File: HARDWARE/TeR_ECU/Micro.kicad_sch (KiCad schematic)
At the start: 23 parts, among them J1 Debug, SW1 RST, U1 STM32F446RETx, Y1 Crystal

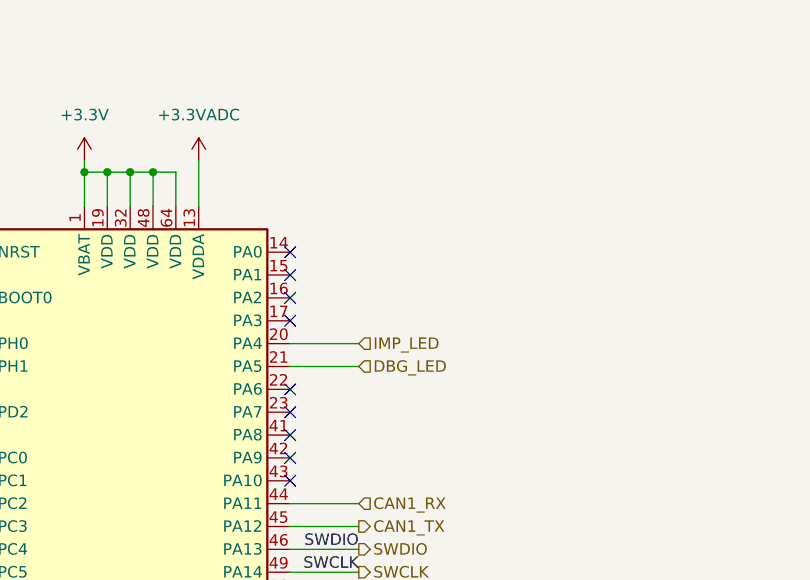
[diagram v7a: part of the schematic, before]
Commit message: Rethought layout and added pulldown to Horn mosfet
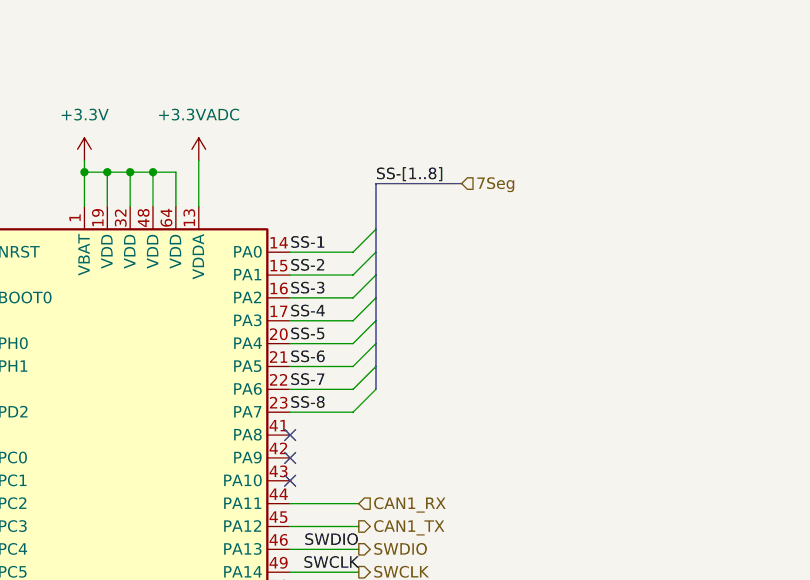
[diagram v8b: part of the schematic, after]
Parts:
- C6: footprint Capacitor_SMD:C_0805_2012Metric -> Capacitor_SMD:C_0402_1005Metric
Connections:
- net SS-1: now reaches U1.14 (PA0)
- net SS-2: now reaches U1.15 (PA1)
- net SS-3: now reaches U1.16 (PA2)
- net SS-4: now reaches U1.17 (PA3)
- net SS-7: now reaches U1.22 (PA6)
- net SS-8: now reaches U1.23 (PA7)
- net DBG_LED renamed SS-6
- net IMP_LED renamed SS-5
- no-connect marks 33 -> 27
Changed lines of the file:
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@@
   (no_connect (at 170.18 81.28))
   (no_connect (at 134.62 114.3))
-  (no_connect (at 170.18 55.88))
   (no_connect (at 134.62 91.44))
-  (no_connect (at 170.18 73.66))
   (no_connect (at 134.62 121.92))
   (no_connect (at 170.18 124.46))
-  (no_connect (at 170.18 63.5))
   (no_connect (at 170.18 127))
-  (no_connect (at 170.18 60.96))
   (no_connect (at 170.18 109.22))
   (no_connect (at 170.18 106.68))
@@
   (no_connect (at 134.62 73.66))
   (no_connect (at 170.18 116.84))
-  (no_connect (at 170.18 58.42))
-  (no_connect (at 170.18 71.12))
   (no_connect (at 170.18 78.74))
   (no_connect (at 134.62 86.36))
   (no_connect (at 134.62 116.84))
+  (bus_entry (at 179.705 68.58) (size -2.54 2.54)
+    (stroke (width 0) (type default))
+  )
+  (bus_entry (at 179.705 53.34) (size -2.54 2.54)
+    (stroke (width 0) (type default))
+  )
+  (bus_entry (at 179.705 60.96) (size -2.54 2.54)
+    (stroke (width 0) (type default))
+  )
+  (bus_entry (at 179.705 63.5) (size -2.54 2.54)
+    (stroke (width 0) (type default))
+  )
+  (bus_entry (at 179.705 55.88) (size -2.54 2.54)
+    (stroke (width 0) (type default))
+  )
+  (bus_entry (at 179.705 71.12) (size -2.54 2.54)
+    (stroke (width 0) (type default))
+  )
+  (bus_entry (at 179.705 66.04) (size -2.54 2.54)
+    (stroke (width 0) (type default))
+  )
+  (bus_entry (at 179.705 58.42) (size -2.54 2.54)
+    (stroke (width 0) (type default))
+  )
   (wire (pts (xy 152.4 46.99) (xy 149.86 46.99))
     (stroke (width 0) (type default))
@@
     (stroke (width 0) (type default))
   )
+  (wire (pts (xy 170.18 66.04) (xy 177.165 66.04))
+    (stroke (width 0) (type default))
+  )
   (wire (pts (xy 34.29 173.99) (xy 38.1 173.99))
     (stroke (width 0) (type default))
@@
     (stroke (width 0) (type default))
   )
-  (wire (pts (xy 170.18 66.04) (xy 177.8 66.04))
+  (bus (pts (xy 179.705 66.04) (xy 179.705 68.58))
+    (stroke (width 0) (type default))
+  )
+  (bus (pts (xy 179.705 58.42) (xy 179.705 60.96))
+    (stroke (width 0) (type default))
+  )
+  (wire (pts (xy 170.18 63.5) (xy 177.165 63.5))
     (stroke (width 0) (type default))
   )
@@
     (stroke (width 0) (type default))
   )
+  (wire (pts (xy 170.18 60.96) (xy 177.165 60.96))
+    (stroke (width 0) (type default))
+  )
   (wire (pts (xy 124.46 66.04) (xy 134.62 66.04))
     (stroke (width 0) (type default))
@@
     (stroke (width 0) (type default))
   )
+  (bus (pts (xy 179.705 53.34) (xy 179.705 55.88))
+    (stroke (width 0) (type default))
+  )
   (polyline (pts (xy 12.7 77.47) (xy 74.93 77.47))
     (stroke (width 0) (type default))
@@
     (stroke (width 0) (type default))
   )
+  (wire (pts (xy 170.18 73.66) (xy 177.165 73.66))
+    (stroke (width 0) (type default))
+  )
   (wire (pts (xy 27.94 91.44) (xy 27.94 88.9))
     (stroke (width 0) (type default))
@@
     (stroke (width 0) (type default))
   )
+  (bus (pts (xy 189.23 48.26) (xy 179.705 48.26))
+    (stroke (width 0) (type default))
+  )
   (wire (pts (xy 38.1 128.27) (xy 38.1 127))
     (stroke (width 0) (type default))
   )
-  (wire (pts (xy 170.18 68.58) (xy 177.8 68.58))
-    (stroke (width 0) (type default))
-  )
   (wire (pts (xy 170.18 91.44) (xy 177.8 91.44))
     (stroke (width 0) (type default))
@@
     (stroke (width 0) (type default))
   )
+  (bus (pts (xy 179.705 63.5) (xy 179.705 66.04))
+    (stroke (width 0) (type default))
+  )
   (wire (pts (xy 33.02 173.99) (xy 34.29 173.99))
     (stroke (width 0) (type default))
@@
     (stroke (width 0) (type default))
   )
+  (wire (pts (xy 170.18 55.88) (xy 177.165 55.88))
+    (stroke (width 0) (type default))
+  )
   (wire (pts (xy 36.83 104.14) (xy 45.72 104.14))
     (stroke (width 0) (type default))
@@
     (stroke (width 0) (type default))
   )
+  (bus (pts (xy 179.705 60.96) (xy 179.705 63.5))
+    (stroke (width 0) (type default))
+  )
   (wire (pts (xy 60.96 128.27) (xy 60.96 127))
     (stroke (width 0) (type default))
@@
     (stroke (width 0) (type default))
   )
+  (bus (pts (xy 179.705 48.26) (xy 179.705 53.34))
+    (stroke (width 0) (type default))
+  )
   (wire (pts (xy 260.35 27.94) (xy 260.35 30.48))
     (stroke (width 0) (type default))
@@
     (stroke (width 0) (type default))
   )
+  (bus (pts (xy 179.705 55.88) (xy 179.705 58.42))
+    (stroke (width 0) (type default))
+  )
   (wire (pts (xy 147.32 45.72) (xy 147.32 46.99))
     (stroke (width 0) (type default))
@@
     (stroke (width 0) (type default))
   )
+  (bus (pts (xy 179.705 68.58) (xy 179.705 71.12))
+    (stroke (width 0) (type default))
+  )
   (wire (pts (xy 52.07 132.08) (xy 52.07 134.62))
     (stroke (width 0) (type default))
   )
+  (wire (pts (xy 170.18 68.58) (xy 177.165 68.58))
+    (stroke (width 0) (type default))
+  )
   (wire (pts (xy 45.72 173.99) (xy 48.26 173.99))
     (stroke (width 0) (type default))
@@
     (stroke (width 0) (type default))
   )
+  (wire (pts (xy 170.18 71.12) (xy 177.165 71.12))
+    (stroke (width 0) (type default))
+  )
   (wire (pts (xy 266.7 38.1) (xy 260.35 38.1))
     (stroke (width 0) (type default))
   )
   (wire (pts (xy 157.48 50.8) (xy 157.48 46.99))
+    (stroke (width 0) (type default))
+  )
+  (wire (pts (xy 170.18 58.42) (xy 177.165 58.42))
     (stroke (width 0) (type default))
   )
@@
     (effects (font (size 1.27 1.27)) (justify right bottom))
   )
+  (label "SS-5" (at 170.18 66.04 0) (fields_autoplaced)
+    (effects (font (size 1.27 1.27)) (justify left bottom))
+  )
   (label "BOOT1" (at 59.69 147.32 180) (fields_autoplaced)
     (effects (font (size 1.27 1.27)) (justify right bottom))
   )
+  (label "SS-[1..8]" (at 179.705 48.26 0) (fields_autoplaced)
+    (effects (font (size 1.27 1.27)) (justify left bottom))
+  )
   (label "OSC_IN" (at 124.46 66.04 0) (fields_autoplaced)
     (effects (font (size 1.27 1.27)) (justify left bottom))
   )
   (label "OSC_OUT" (at 124.46 68.58 0) (fields_autoplaced)
+    (effects (font (size 1.27 1.27)) (justify left bottom))
+  )
+  (label "SS-6" (at 170.18 68.58 0) (fields_autoplaced)
+    (effects (font (size 1.27 1.27)) (justify left bottom))
+  )
+  (label "SS-3" (at 170.18 60.96 0) (fields_autoplaced)
     (effects (font (size 1.27 1.27)) (justify left bottom))
   )
@@
     (effects (font (size 1.27 1.27)) (justify right bottom))
   )
+  (label "SS-1" (at 170.18 55.88 0) (fields_autoplaced)
+    (effects (font (size 1.27 1.27)) (justify left bottom))
+  )
+  (label "SS-4" (at 170.18 63.5 0) (fields_autoplaced)
+    (effects (font (size 1.27 1.27)) (justify left bottom))
+  )
   (label "NRST" (at 124.46 55.88 0) (fields_autoplaced)
     (effects (font (size 1.27 1.27)) (justify left bottom))
@@
     (effects (font (size 1.27 1.27)) (justify right bottom))
   )
+  (label "SS-7" (at 170.18 71.12 0) (fields_autoplaced)
+    (effects (font (size 1.27 1.27)) (justify left bottom))
+  )
+  (label "SS-8" (at 170.18 73.66 0) (fields_autoplaced)
+    (effects (font (size 1.27 1.27)) (justify left bottom))
+  )
+  (label "SS-2" (at 170.18 58.42 0) (fields_autoplaced)
+    (effects (font (size 1.27 1.27)) (justify left bottom))
+  )
   (label "SWDIO" (at 177.8 88.9 180) (fields_autoplaced)
     (effects (font (size 1.27 1.27)) (justify right bottom))
@@
     (effects (font (size 1.27 1.27)) (justify left))
   )
-  (hierarchical_label "IMP_LED" (shape input) (at 177.8 66.04 0) (fields_autoplaced)
+  (hierarchical_label "7Seg" (shape input) (at 189.23 48.26 0) (fields_autoplaced)
     (effects (font (size 1.27 1.27)) (justify left))
   )
@@
   )
   (hierarchical_label "CAN1_RX" (shape input) (at 177.8 83.82 0) (fields_autoplaced)
-    (effects (font (size 1.27 1.27)) (justify left))
-  )
-  (hierarchical_label "DBG_LED" (shape input) (at 177.8 68.58 0) (fields_autoplaced)
     (effects (font (size 1.27 1.27)) (justify left))
   )
@@
       (effects (font (size 1.27 1.27)) (justify right))
     )
-    (property "Footprint" "Capacitor_SMD:C_0805_2012Metric" (at 63.8048 24.13 0)
-      (effects (font (size 1.27 1.27)) hide)
-    )
+    (property "Footprint" "Capacitor_SMD:C_0402_1005Metric" (at 63.8048 24.13 0)
+      (effects (font (size 1.27 1.27)) hide)
+    )
